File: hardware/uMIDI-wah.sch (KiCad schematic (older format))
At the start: 30 parts, among them IC1 Opamp_Dual_Generic, IC2 L78L09_SOT89, X1 AudioJack3_Switch, X3 AudioJack3_Switch, X4 Conn_01x10

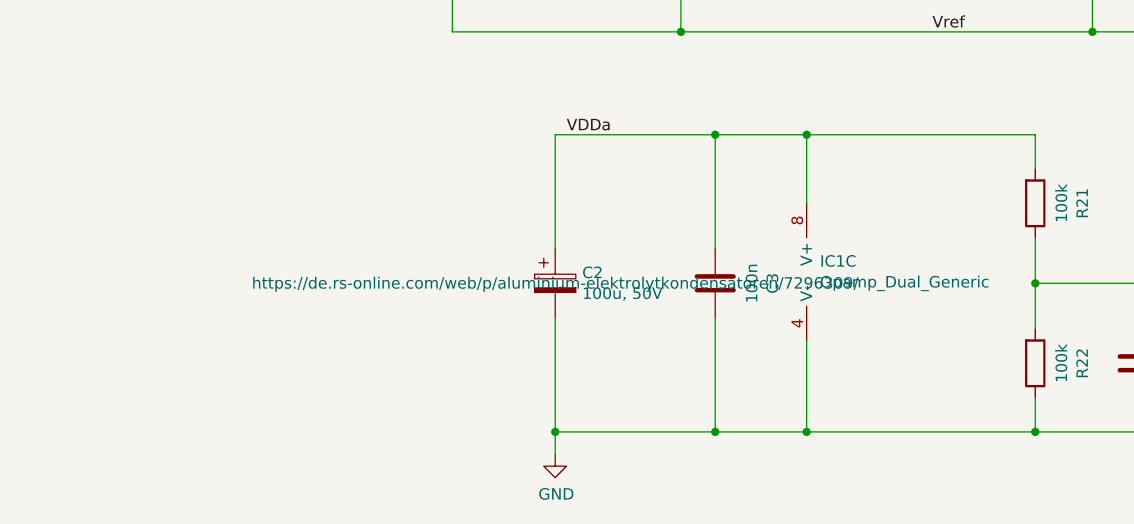
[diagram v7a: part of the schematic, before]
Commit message: Revision BOM: Get low-tech parts from Reichelt
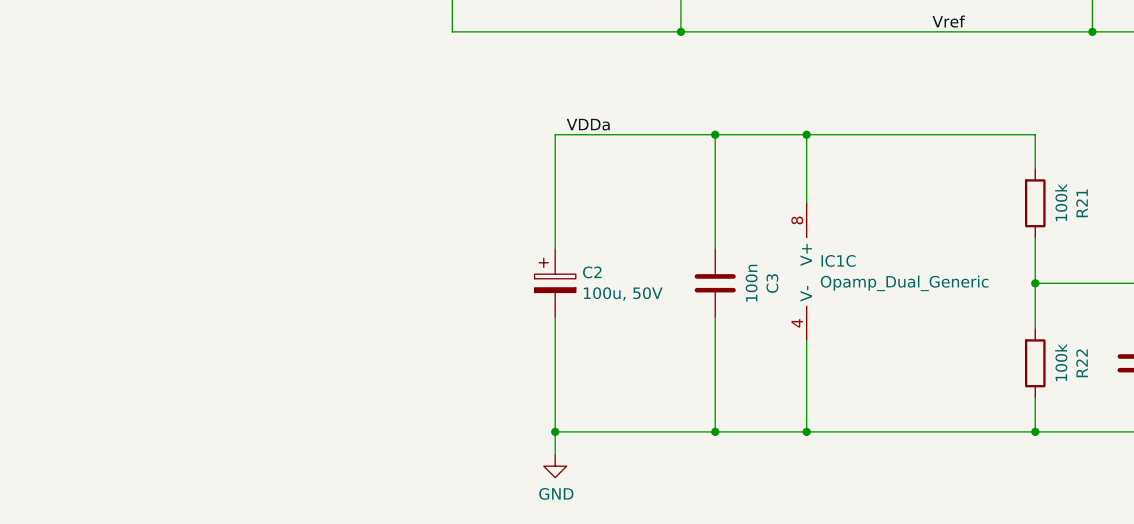
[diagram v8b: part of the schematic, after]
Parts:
- C1, C12, C6: Manufacturer (none) -> TDK; Manufacturer Part Number (none) -> C2012X5R1C226K125AC; Supplier Link https://de.rs-online.com/web/p/keramik-vielschichtkondensat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 -> https://www.rsonline-privat.de/Products/ProductDetail/TDK-C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; Supplier Part Number 169-2721 -> 7883023
- C13, C14, C3: Manufacturer (none) -> YAGEO; Manufacturer Part Number (none) -> CC0805KRX7R9BB104; Supplier RS -> Reichelt; Supplier Link https://de.rs-online.com/web/p/keramik-vielschichtkondensat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 -> https://www.reichelt.de/smd-vielschicht-keramikkondensator-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; Supplier Part Number 170-0041 -> X7R-G0805 100N
- C2: Manufacturer (none) -> Panasonic; Manufacturer Part Number (none) -> EEEFTH101XAP; Supplier RS -> Reichelt; Supplier Link https://de.rs-online.com/web/p/aluminium-elektrolytkondensa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 -> https://www.reichelt.de/elko-smd-100-uf-50-v-105-c-ft-v-100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; Supplier Part Number 729-6309 -> FT-V 100U 50
- C4: Manufacturer (none) -> KEMET; Manufacturer Part Number (none) -> C0805C333K5RAC7025; Supplier RS -> Reichelt; Supplier Link https://de.rs-online.com/web/p/keramik-vielschichtkondensat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 -> https://www.reichelt.de/vielschicht-kerko-33nf-50v-125-c-ke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; Supplier Part Number 169-6231 -> KEM X7R0805 33N
- IC1: Supplier RS -> Reichelt; Supplier Link https://de.rs-online.com/web/p/operationsverstarker/0304239/ -> https://www.reichelt.de/operationsverstaerker-2-fach-dip-8-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; Supplier Part Number 304-239 -> TL 072 DIP
- IC2: Supplier Link https://de.rs-online.com/web/p/spannungs-linearregler/68694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 -> https://www.rsonline-privat.de/Products/ProductDetail/L78L0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; Supplier Part Number 686-9467 -> 6869467
- LDR1, LDR2: Supplier Link https://de.rs-online.com/web/p/fotowiderstande-ldr/9146714/ -> https://www.rsonline-privat.de/Products/ProductDetail/Luna-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; Supplier Part Number 914-6714 -> 9146714
- R1, R21, R22, R3, R8: Manufacturer (none) -> YAGEO; Manufacturer Part Number (none) -> RC0805FR-07100KL; Supplier RS -> Reichelt; Supplier Link https://de.rs-online.com/web/p/smd-widerstande/8046607/ -> https://www.reichelt.de/smd-widerstand-0805-100-kohm-125-mw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; Supplier Part Number 804-6607 -> SMD-0805 100K
- R10, R11: Manufacturer (none) -> TE Connectivity; Manufacturer Part Number (none) -> RH73H2A100MKTN; Supplier Link https://de.rs-online.com/web/p/smd-widerstande/2945062/ -> https://www.rsonline-privat.de/Products/ProductDetail/TE-Co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; Supplier Part Number 294-5062 -> 2945062
- R2, R4: Manufacturer (none) -> YAGEO; Manufacturer Part Number (none) -> RC0805FR-071KL; Supplier RS -> Reichelt; Supplier Link https://de.rs-online.com/web/p/smd-widerstande/8046449/ -> https://www.reichelt.de/smd-widerstand-0805-1-0-kohm-125-mw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; Supplier Part Number 804-6449 -> SMD-0805 1,00K
- RV1, RV2, RV3: Supplier Link https://de.rs-online.com/web/p/abgleichwiderstande/3746844/ -> https://www.rsonline-privat.de/Products/ProductDetail/Visha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; Supplier Part Number 374-6844 -> 3746844
- X1, X3: Manufacturer RS -> RS PRO; Supplier Link https://de.rs-online.com/web/p/klinkenstecker/9131037/ -> https://www.rsonline-privat.de/Products/ProductDetail/Klink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; Supplier Part Number 913-1037 -> 9131037
- X4: Manufacturer Wuerth -> Wurth Elektronik; Supplier Link https://de.rs-online.com/web/p/leiterplatten-header/1216784/ -> https://www.rsonline-privat.de/Products/ProductDetail/Wurth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; Supplier Part Number 121-6784 -> 7718354
